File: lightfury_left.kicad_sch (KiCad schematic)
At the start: 81 parts, among them U1 TLV61070ADBV, U2 SN74LV1T126DBVR

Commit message: Added capacitors for 5v load smoothing.
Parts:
- added C3: 100nF, Capacitor_SMD:C_0603_1608Metric, symbol Device:C
- added C4, C5: 10µF, Capacitor_SMD:C_0603_1608Metric, symbol Device:C
- MCU1: symbol huntercooh:nice_nano -> huntercook:nice_nano
- RE1: symbol huntercooh:RotaryEncoder_Switch -> huntercook:RotaryEncoder_Switch
- S1, S10, S11, S12, S13, S14, S15, S16, S17, S18, S19, S2, S20, S21, S22, S23, S24, S25, S26, S27, S3, S4, S5, S6, S7, S8, S9: symbol huntercooh:PG1316S -> huntercook:PG1316S
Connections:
- net 5V: now also C3.1, C4.1, C5.1
- net GND: now also C3.2, C4.2, C5.2

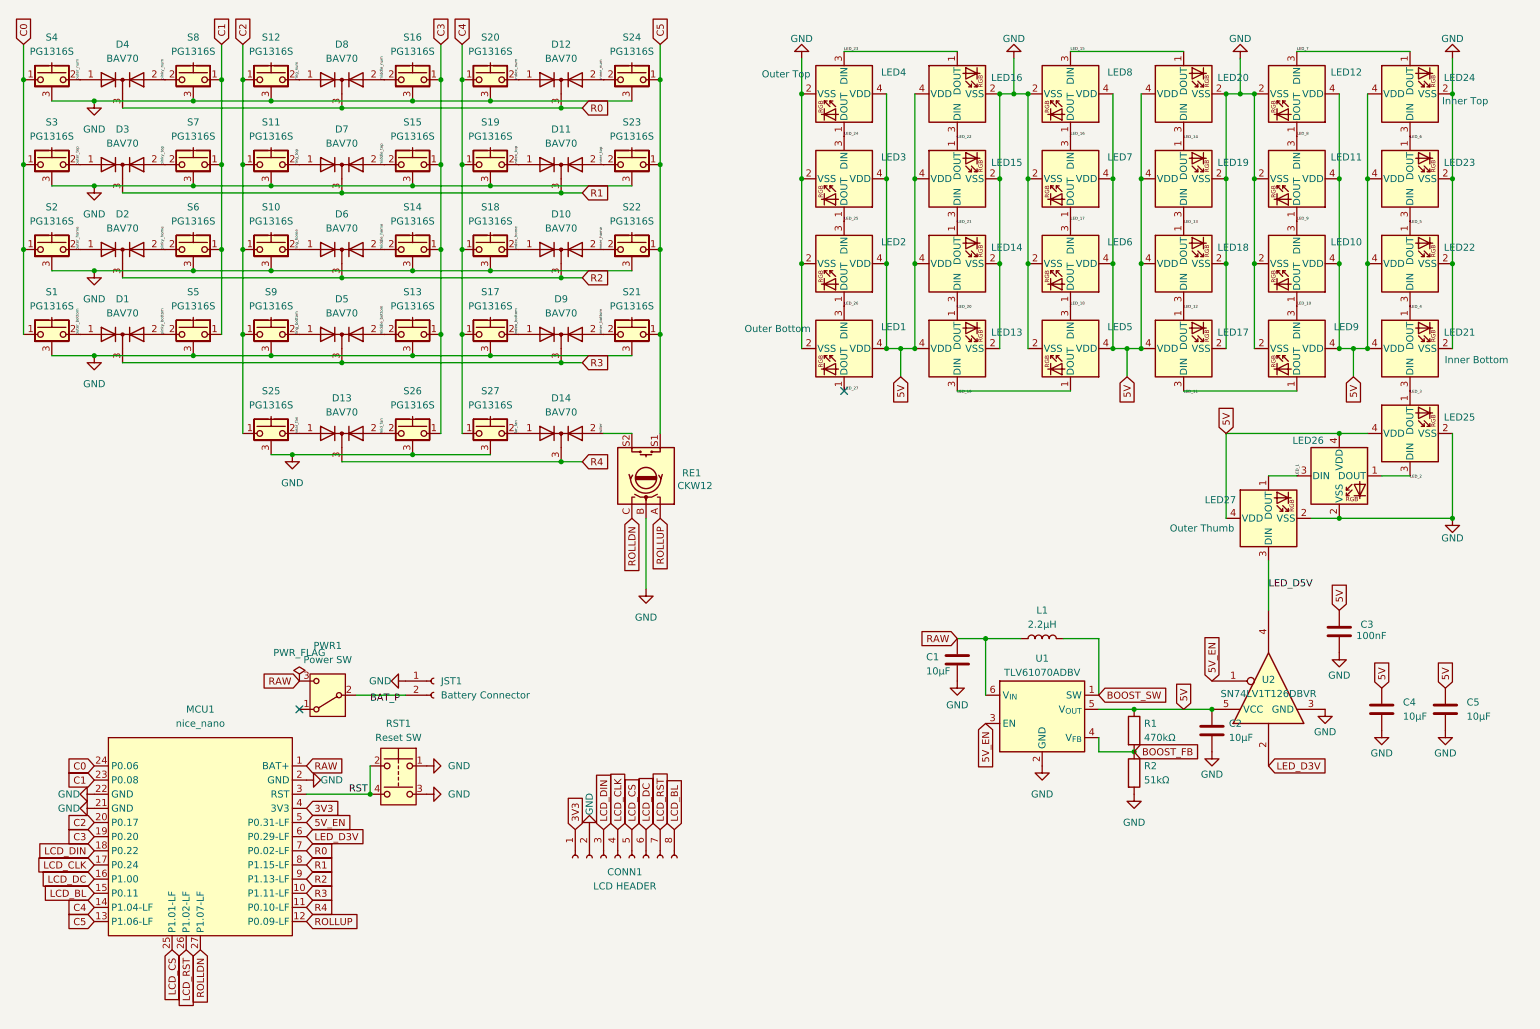
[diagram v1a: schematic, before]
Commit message: Add LCSC field and populate for BOM.
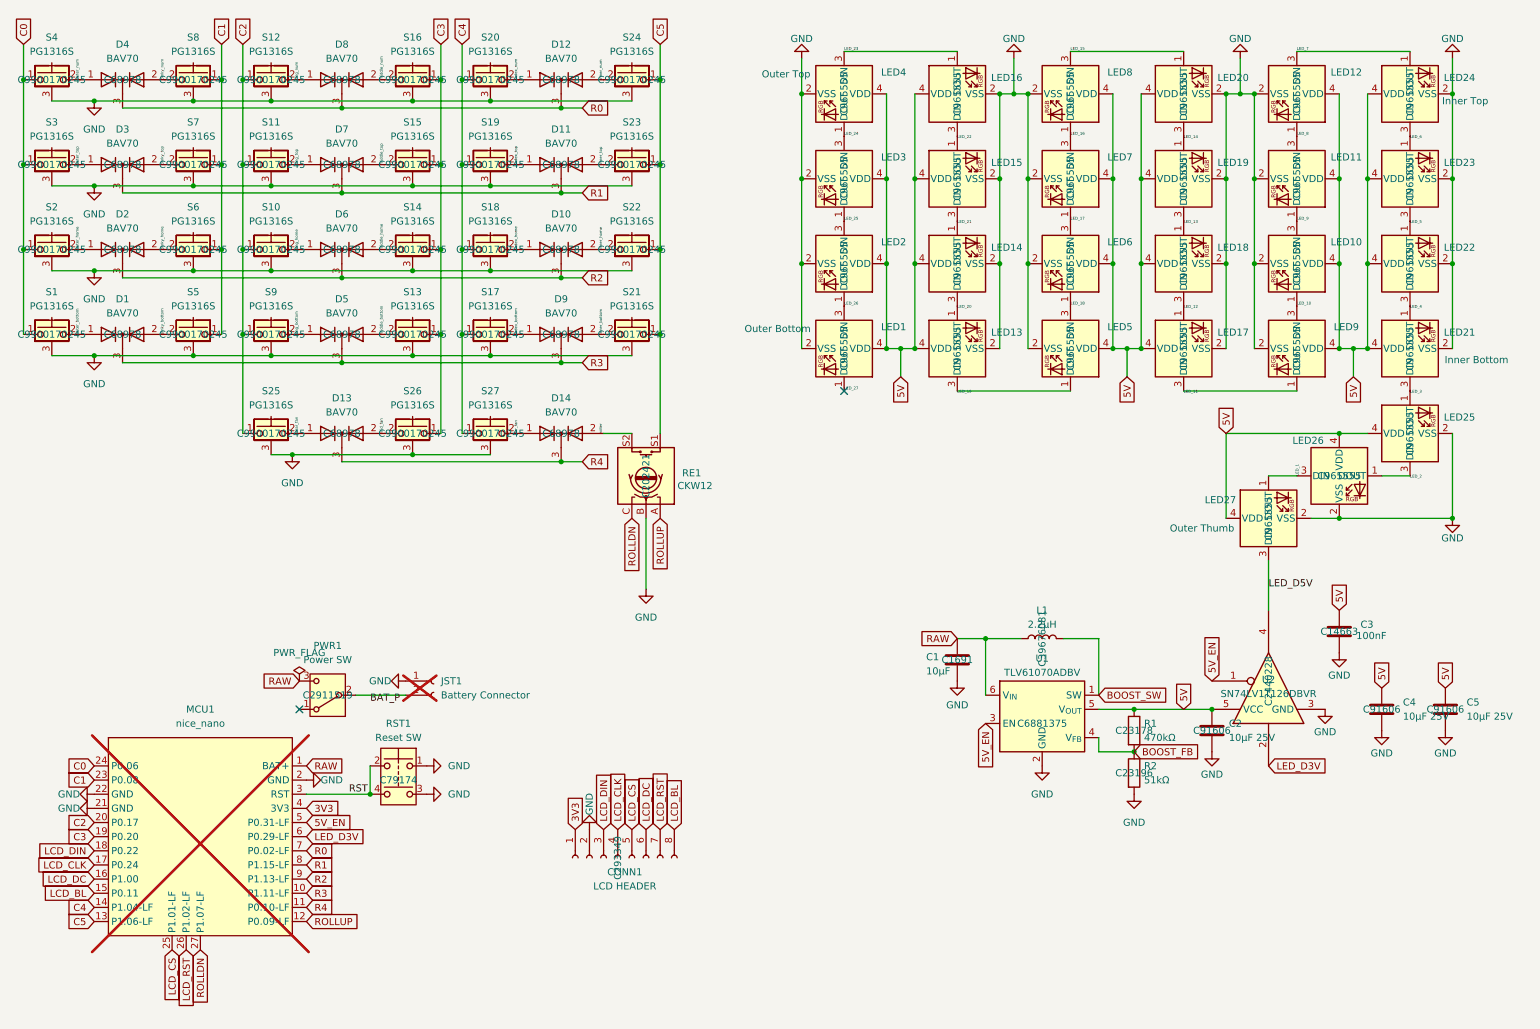
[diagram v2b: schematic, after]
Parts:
- C1: LCSC (none) -> C1691
- C2: value 10μF -> 10μF 25V; LCSC (none) -> C91606
- C3: LCSC (none) -> C14663
- C4, C5: value 10µF -> 10µF 25V; LCSC (none) -> C91606
- CONN1: LCSC (none) -> C293349
- D1, D10, D11, D12, D13, D14, D2, D3, D4, D5, D6, D7, D8, D9: LCSC (none) -> C68978
- JST1: now not fitted; now left out of the parts list
- L1: LCSC (none) -> C39676081
- LED1, LED10, LED11, LED12, LED13, LED14, LED15, LED16, LED17, LED18, LED19, LED2, LED20, LED21, LED22, LED23, LED24, LED25, LED26, LED27, LED3, LED4, LED5, LED6, LED7, LED8, LED9: LCSC (none) -> C965555
- MCU1: now not fitted
- PWR1: LCSC (none) -> C2911519
- R1: LCSC (none) -> C23178
- R2: LCSC (none) -> C23196
- RE1: LCSC (none) -> C202421
- RST1: LCSC (none) -> C79174
- S1, S10, S11, S12, S13, S14, S15, S16, S17, S18, S19, S2, S20, S21, S22, S23, S24, S25, S26, S27, S3, S4, S5, S6, S7, S8, S9: LCSC (none) -> C9900170245
- U1: LCSC (none) -> C6881375
- U2: LCSC (none) -> C2440228
